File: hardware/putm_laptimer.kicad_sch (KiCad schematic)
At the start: 44 parts, among them J1 Conn_01x22, J10 Conn_01x07, J11 Conn_01x07, J12 Conn_01x05, J13 Conn_01x05, J14 2091-1376, J2 Conn_01x22, J3 Conn_01x22, J4 Conn_01x22, J7 Conn_02x05_Odd_Even, J8 Conn_01x09, J9 M80-5001805

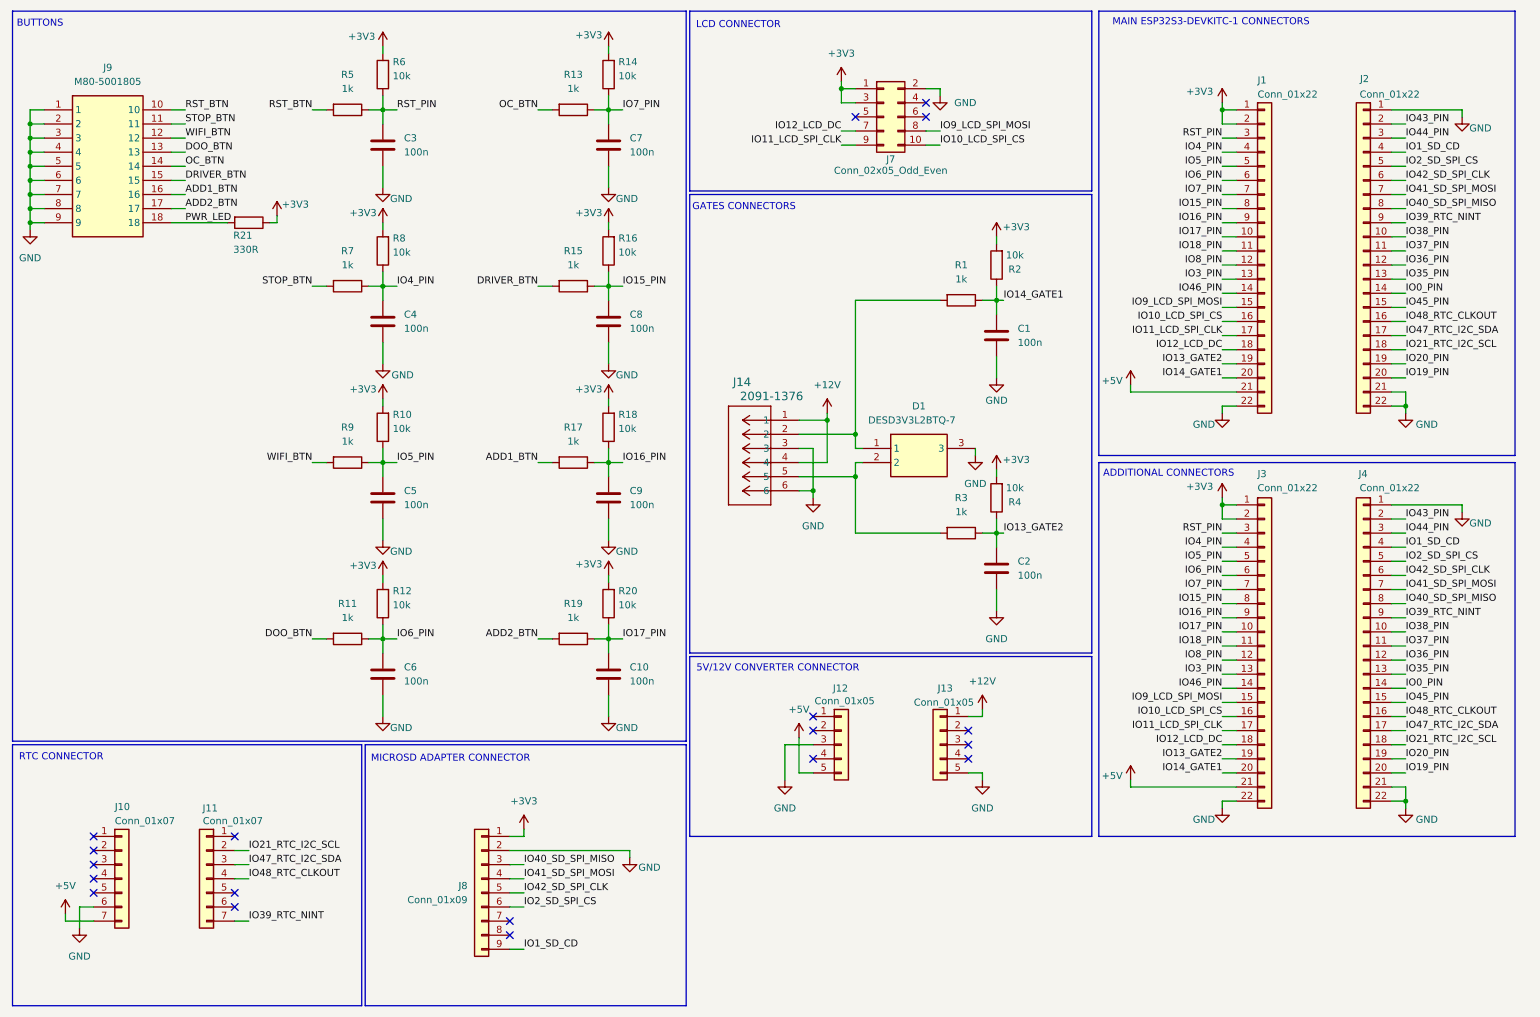
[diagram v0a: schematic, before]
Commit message: Added modules info and links to connector schematics
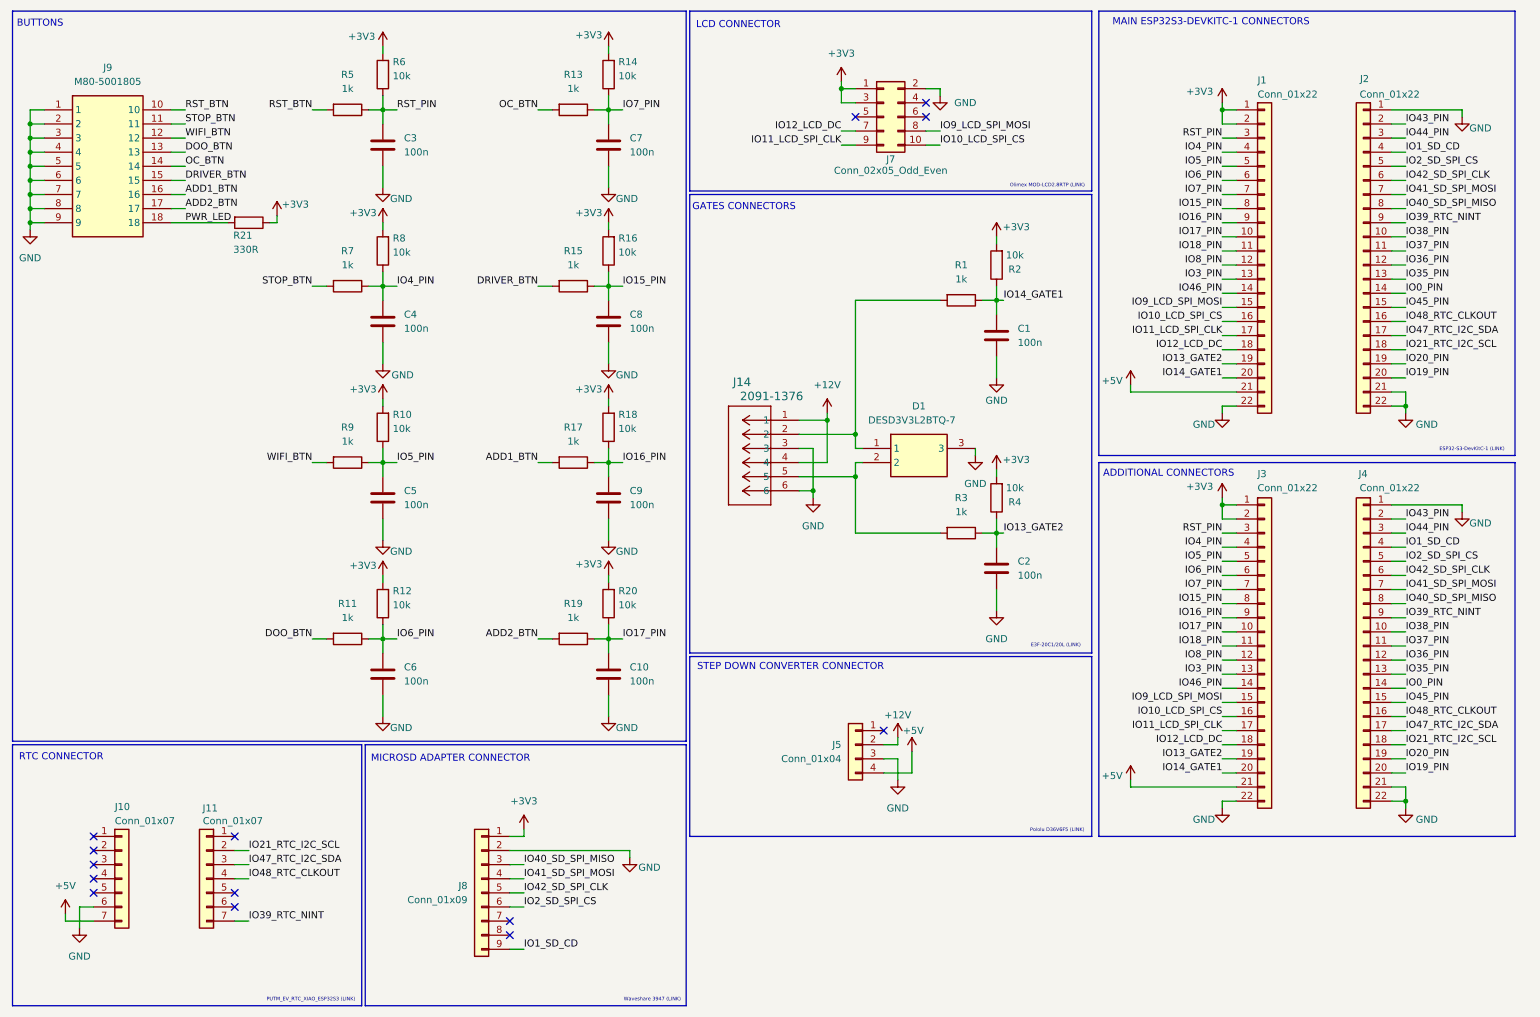
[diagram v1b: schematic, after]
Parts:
- removed J12, J13: Conn_01x05, Connector_PinSocket_2.00mm:PinSocket_1x05_P2.00mm_Vertical, symbol Connector_Generic:Conn_01x05
- added J5: Conn_01x04, symbol Connector_Generic:Conn_01x04
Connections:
- net +12V: now also J5.2 (Pin_2)
- net +5V: now also J5.4 (Pin_4)
- net GND: now also J5.3 (Pin_3)
- no-connect marks 19 -> 14
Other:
- note added: "E3F-20C1/20L (LINK)"
- note added: "ESP32-S3-DevKitC-1 (LINK)"
- note added: "Olimex MOD-LCD2.8RTP (LINK)"
- note added: "PUTM_EV_RTC_XIAO_ESP32S3 (LINK)"
- note added: "Pololu D36V6F5 (LINK)"
- note added: "STEP DOWN CONVERTER CONNECTOR"
- note added: "Waveshare 3947 (LINK)"
- note removed: "5V/12V CONVERTER CONNECTOR"

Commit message: Changed layout, changed gate connector, added 12V battery connector and buck converter pins
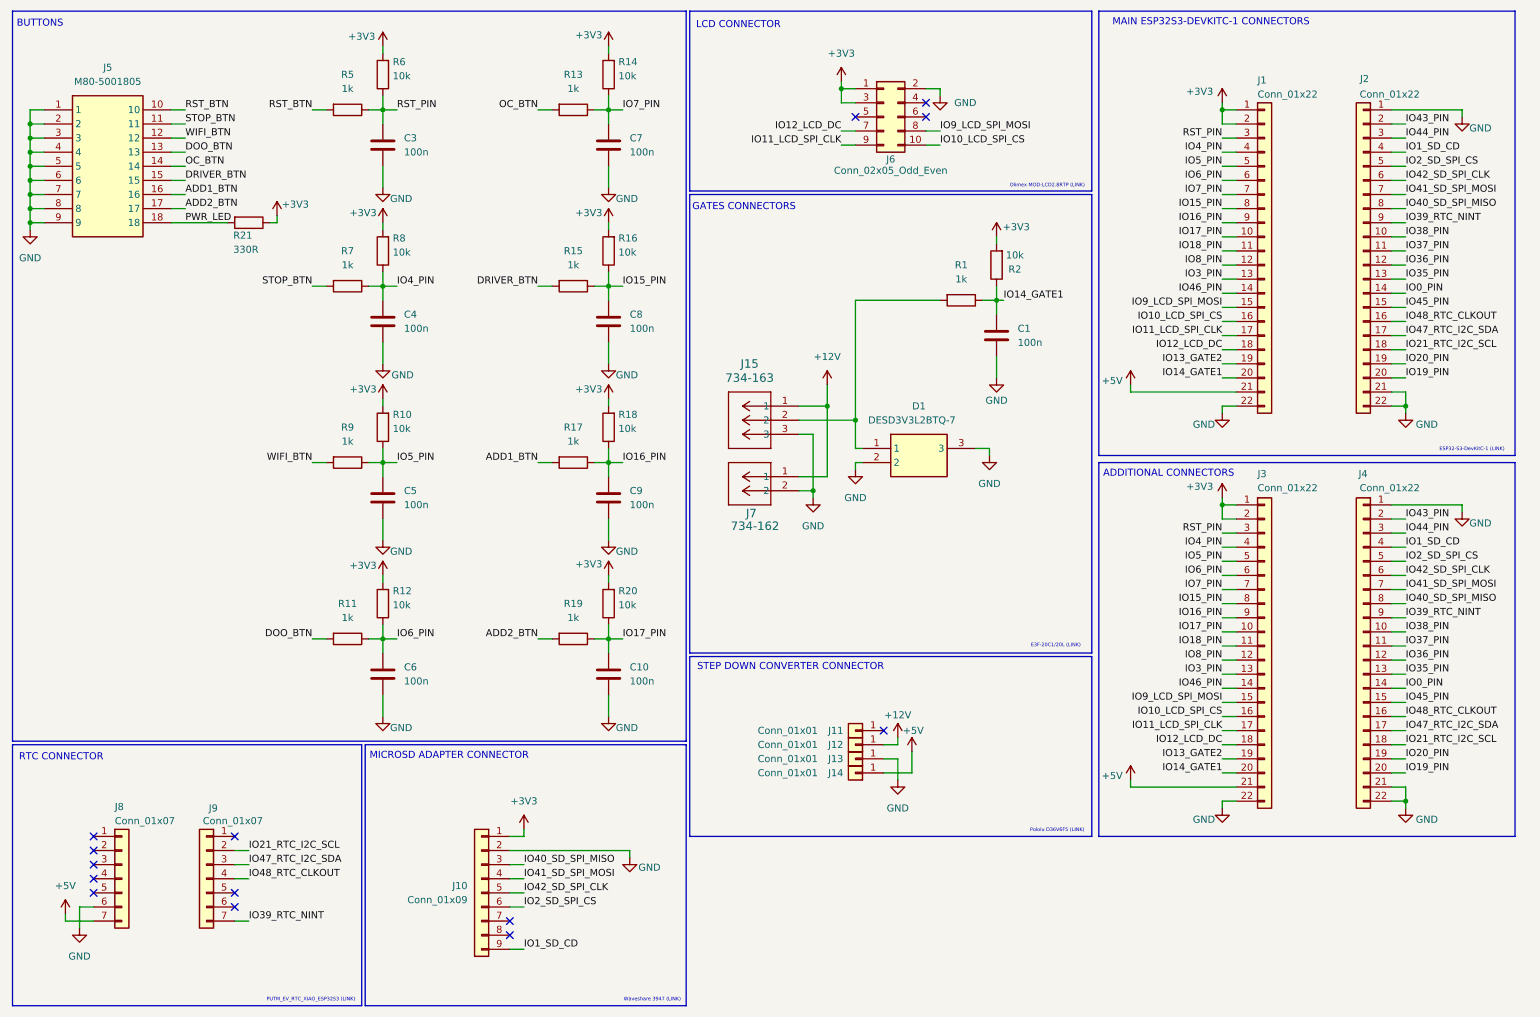
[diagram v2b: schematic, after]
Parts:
- removed C2: 100n, Capacitor_SMD:C_0603_1608Metric, symbol Device:C
- removed J14: 2091-1376, Footprint:CONN6_2091-1376_WAG, symbol 2026-01-25_23-06-05:2091-1376
- removed J5: Conn_01x04, symbol Connector_Generic:Conn_01x04
- removed R3: 1k, Resistor_SMD:R_0603_1608Metric, symbol Device:R
- removed R4: 10k, Resistor_SMD:R_0603_1608Metric, symbol Device:R
- added J11, J12, J13, J14: Conn_01x01, TestPoint:TestPoint_THTPad_D1.5mm_Drill0.7mm, symbol Connector_Generic:Conn_01x01
- added J15: 734-163, CONN3_734-163_WAG, symbol 2026-02-02_14-21-35:734-163
- added J7: 734-162, CONN2_734-162_WAG, symbol 2026-02-02_14-12-37:734-162
- renumbered J8 to J10, J9 to J5, J7 to J6, J10 to J8, J11 to J9
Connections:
- net +12V: now also J12.1 (Pin_1), J15.1, J7.1
- net +5V: now also J14.1 (Pin_1)
- net GND: now also D1.2, J13.1 (Pin_1), J15.3, J7.2
- net at D1.1, R1.2: now also J15.2

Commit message: Fixed schematics
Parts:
- renumbered J9 to J10, J10 to J11, J11 to J12, J12 to J13, J13 to J14, J14 to J15, J15 to J7, J7 to J8, J8 to J9
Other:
- note added: "12V BATTERY CONNECTOR"
- note added: "CONDUCTOR CONNECTOR WAGO 2734-102 (LINK)"
- note added: "CONDUCTOR CONNECTOR WAGO 2734-103 (LINK)"
- note added: "GATE CONNECTOR"
- note removed: "GATES CONNECTORS"
- moved on the sheet: C1, D1, J7, J8, R1, R2

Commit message: Fixed pcb layout
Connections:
- net IO13_GATE2 renamed IO13
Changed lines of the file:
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@@
 		)
 	)
-	(label "IO13_GATE2"
+	(label "IO13"
 		(at 231.14 77.47 180)
 		(effects
 			(font
 				(size 1.27 1.27)
+				(color 132 132 132 1)
 			)
 			(justify right bottom)
@@
 		)
 	)
-	(label "IO13_GATE2"
+	(label "IO13"
 		(at 231.14 148.59 180)
 		(effects
 			(font
 				(size 1.27 1.27)
-			)
-			(justify right bottom)
+				(color 132 132 132 1)
+			)
+			(justify right bottom)

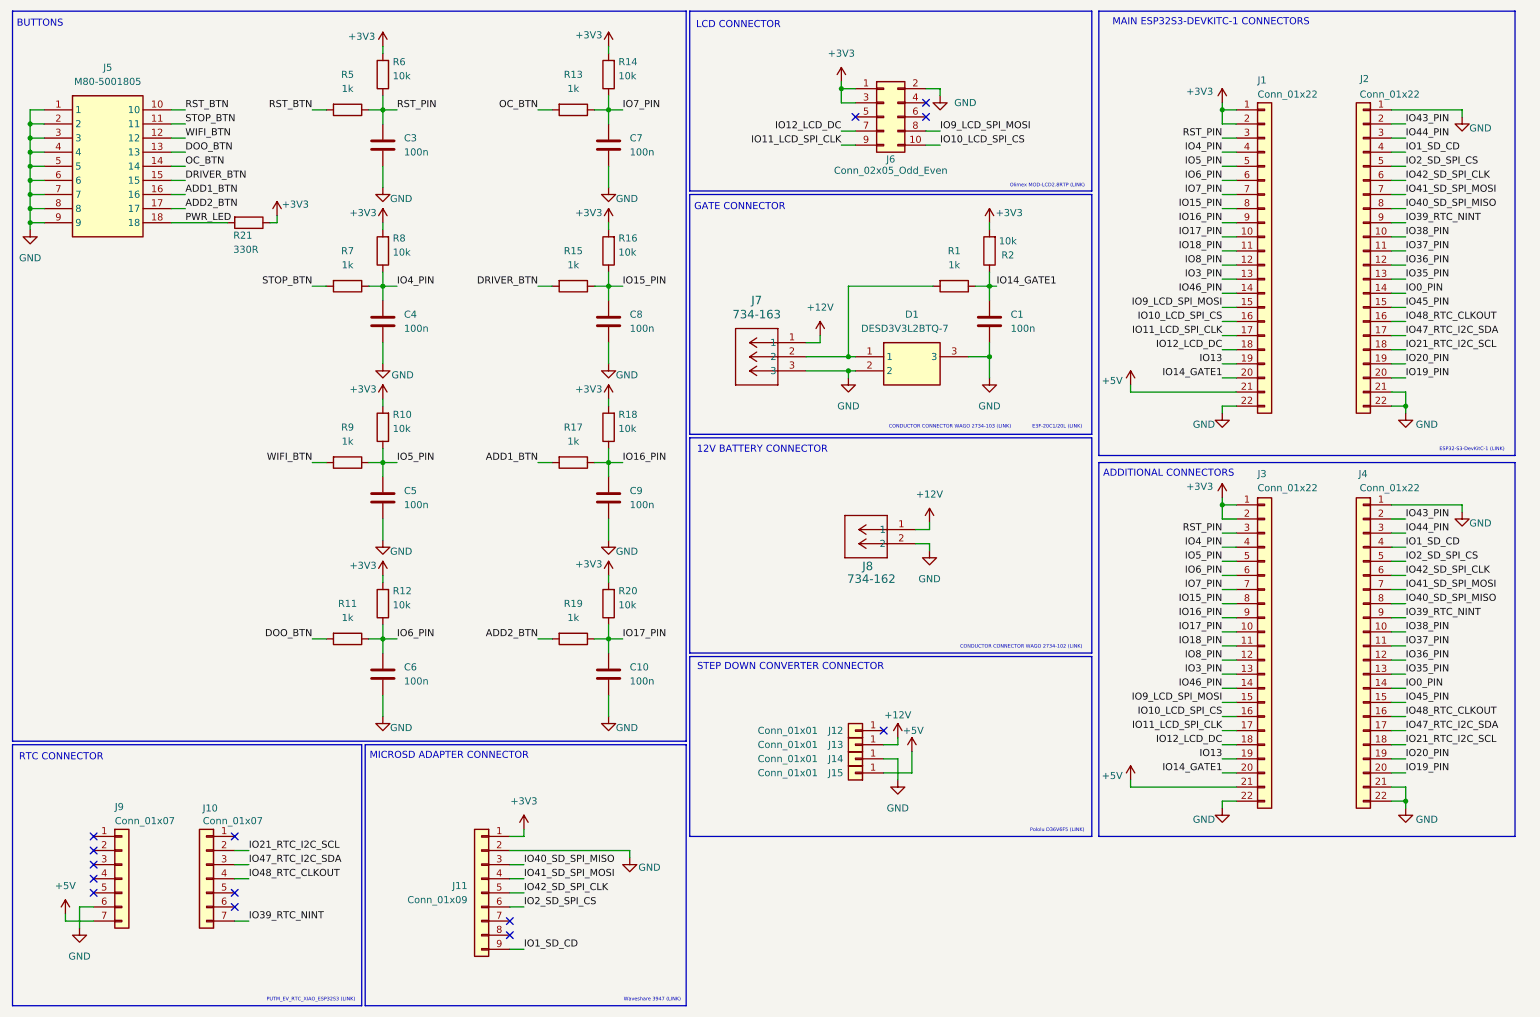
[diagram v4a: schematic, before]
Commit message: Changed connectors
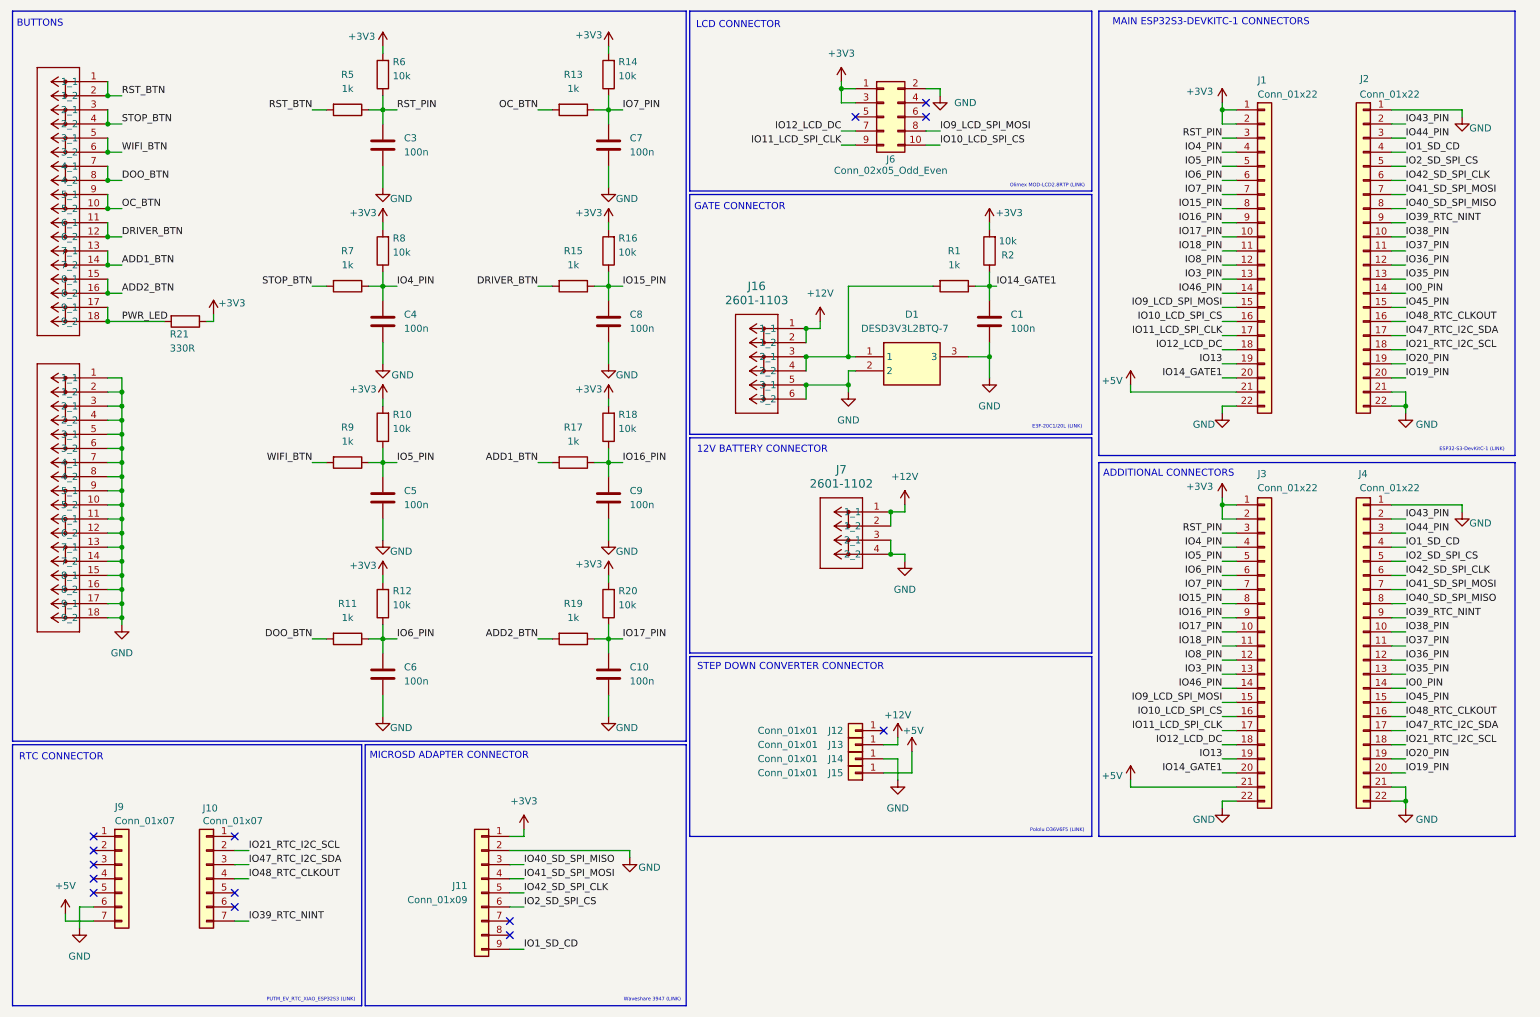
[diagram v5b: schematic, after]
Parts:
- removed J5: M80-5001805, Footprint:M80-50018YY_2, symbol M80-5001805:M80-5001805
- removed J7: 734-163, CONN3_734-163_WAG, symbol 2026-02-02_14-21-35:734-163
- removed J8: 734-162, CONN2_734-162_WAG, symbol 2026-02-02_14-12-37:734-162
- added J16: 2601-1103, CONN3_2601-1103_WAG, symbol 2026-02-04_11-25-15:2601-1103
- added J5, J8: 2601-3109, CONN9_2601-3109_WAG, symbol 2026-02-04_12-45-28:2601-3109
- added J7: 2601-1102, CONN2_2601-1102_WAG, symbol 2026-02-04_12-17-39:2601-1102
- J12, J13, J14, J15: footprint TestPoint:TestPoint_THTPad_D1.5mm_Drill0.7mm -> TestPoint:TestPoint_THTPad_D2.0mm_Drill1.0mm
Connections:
- net +12V: now also J16.1 (1_1), J16.2 (1_2), J7.1 (1_1), J7.2 (1_2)
- net ADD1_BTN: now also J8.13 (7_1), J8.14 (7_2)
- net ADD2_BTN: now also J8.15 (8_1), J8.16 (8_2)
- net DOO_BTN: now also J8.7 (4_1), J8.8 (4_2)
- net DRIVER_BTN: now also J8.11 (6_1), J8.12 (6_2)
- net GND: now also J16.5 (3_1), J16.6 (3_2), J5.1 (1_1), J5.10 (5_2), J5.11 (6_1), J5.12 (6_2), J5.13 (7_1), J5.14 (7_2), J5.15 (8_1), J5.16 (8_2), J5.17 (9_1), J5.18 (9_2), J5.2 (1_2), J5.3 (2_1), J5.4 (2_2), J5.5 (3_1), J5.6 (3_2), J5.7 (4_1), J5.8 (4_2), J5.9 (5_1), J7.3 (2_1), J7.4 (2_2)
- net OC_BTN: now also J8.10 (5_2), J8.9 (5_1)
- net PWR_LED: now also J8.17 (9_1), J8.18 (9_2)
- net RST_BTN: now also J8.1 (1_1), J8.2 (1_2)
- net STOP_BTN: now also J8.3 (2_1), J8.4 (2_2)
- net WIFI_BTN: now also J8.5 (3_1), J8.6 (3_2)
- net at D1.1, R1.2: now also J16.3 (2_1), J16.4 (2_2)
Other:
- note removed: "CONDUCTOR CONNECTOR WAGO 2734-102 (LINK)"
- note removed: "CONDUCTOR CONNECTOR WAGO 2734-103 (LINK)"
- moved on the sheet: R21
